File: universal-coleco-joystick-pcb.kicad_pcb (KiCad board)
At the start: 2 copper layers, 108 x 62.3 mm, 50 parts, among them J1 Sanwa Joystick, J2 DE9_Receptacle, J3 Conn_01x09_Socket, J4 Opt'l Numbers, SW1 Arm, SW10 2, SW11 #, SW12 9, SW13 6, SW14 3, SW2 Fire, SW3 *, SW4 7, SW5 1, SW6 4, SW7 0, SW8 8, SW9 5

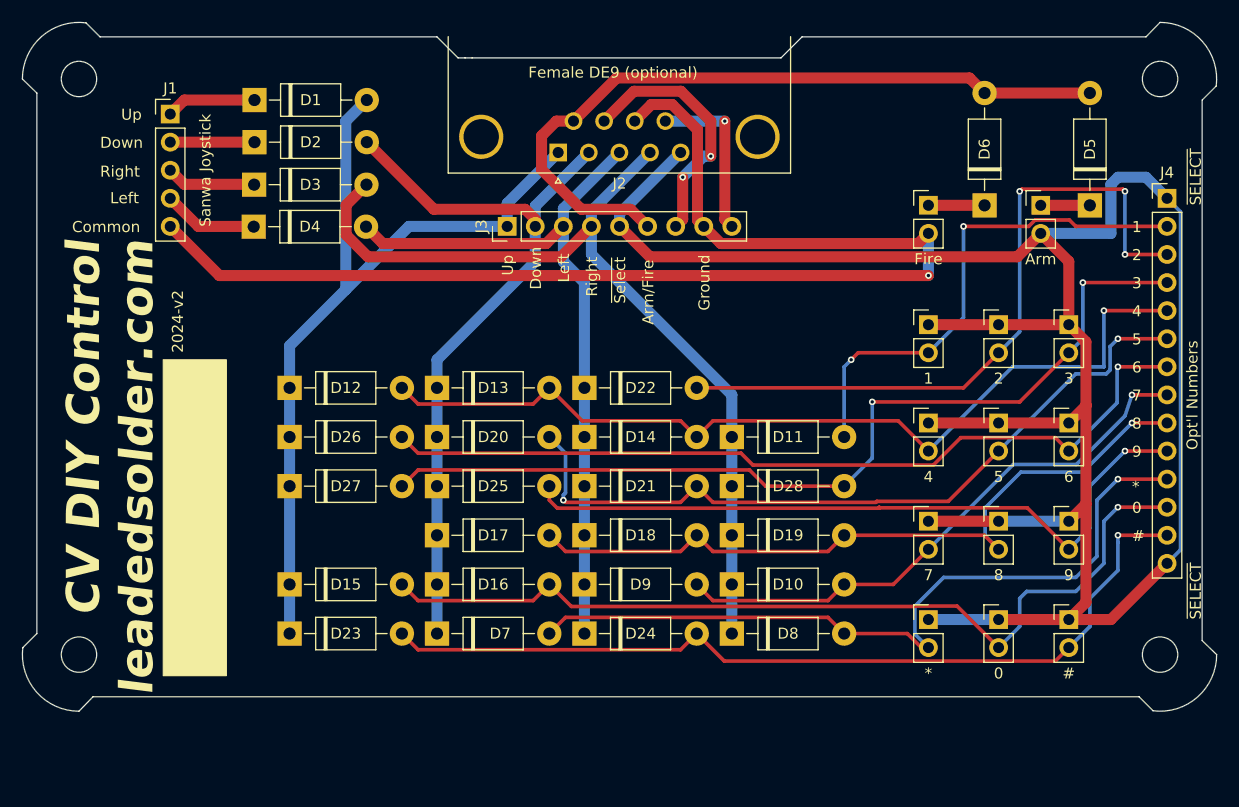
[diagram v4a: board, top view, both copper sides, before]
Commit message: Diodes flipped, board shrunk below 100x100
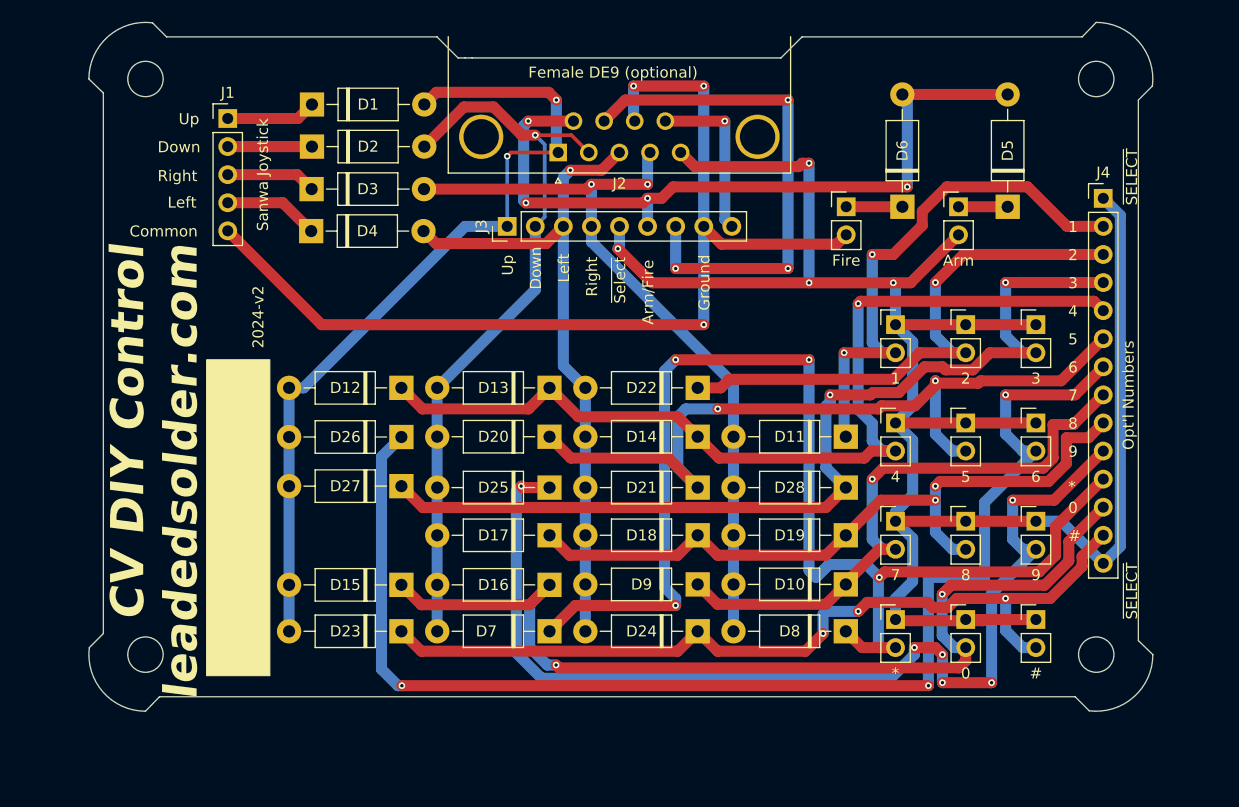
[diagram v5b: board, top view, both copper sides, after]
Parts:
- moved D8 10.3 mm to (156.4, 116.0), turned to 180 degrees
- moved D28 10.3 mm to (156.4, 103.0), turned to 180 degrees
- moved D11 10.3 mm to (156.4, 98.4), turned to 180 degrees
- moved D10 10.3 mm to (156.4, 111.8), turned to 180 degrees
- moved D19 10.3 mm to (156.4, 107.3), turned to 180 degrees
- moved D24 10.2 mm to (143.0, 116.0), turned to 180 degrees
- moved D21 10.2 mm to (143.0, 103.0), turned to 180 degrees
- moved D14 10.2 mm to (143.0, 98.4), turned to 180 degrees
- moved D18 10.2 mm to (143.0, 107.3), turned to 180 degrees
- moved D22 10.2 mm to (143.0, 94.0), turned to 180 degrees
- moved D9 10.2 mm to (143.0, 111.8), turned to 180 degrees
- moved D7 10.2 mm to (129.6, 116.0), turned to 180 degrees
- moved D25 10.2 mm to (129.6, 103.0), turned to 180 degrees
- moved D16 10.2 mm to (129.6, 111.8), turned to 180 degrees
- moved D20 10.2 mm to (129.6, 98.4), turned to 180 degrees
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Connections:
- D10 pad 1: /Right -> /KP_7
- D10 pad 2: /KP_7 -> /Right
- D11 pad 1: /Right -> /KP_1
- D11 pad 2: /KP_1 -> /Right
- D12 pad 1: /Up -> /KP_4
- D12 pad 2: /KP_4 -> /Up
- D13 pad 1: /Down -> /KP_4
- D13 pad 2: /KP_4 -> /Down
- D14 pad 1: /Left -> /KP_4
- D14 pad 2: /KP_4 -> /Left
- D15 pad 1: /Up -> /KP_0
- D15 pad 2: /KP_0 -> /Up
- D16 pad 1: /Down -> /KP_0
- D16 pad 2: /KP_0 -> /Down
- D17 pad 1: /Down -> /KP_8
- D17 pad 2: /KP_8 -> /Down
- D18 pad 1: /Left -> /KP_8
- D18 pad 2: /KP_8 -> /Left
- D19 pad 1: /Right -> /KP_8
- D19 pad 2: /KP_8 -> /Right
- D20 pad 1: /Down -> /KP_5
- D20 pad 2: /KP_5 -> /Down
- D21 pad 1: /Left -> /KP_5
- D21 pad 2: /KP_5 -> /Left
- D22 pad 1: /Left -> /KP_2
- D22 pad 2: /KP_2 -> /Left
- D23 pad 1: /Up -> /KP_OCTOTHORPE
- D23 pad 2: /KP_OCTOTHORPE -> /Up
- D24 pad 1: /Left -> /KP_OCTOTHORPE
- D24 pad 2: /KP_OCTOTHORPE -> /Left
- D25 pad 1: /Down -> /KP_9
- D25 pad 2: /KP_9 -> /Down
- D26 pad 1: /Up -> /KP_6
- D26 pad 2: /KP_6 -> /Up
- D27 pad 1: /Up -> /KP_3
- D27 pad 2: /KP_3 -> /Up
- D28 pad 1: /Right -> /KP_3
- D28 pad 2: /KP_3 -> /Right
- D7 pad 1: /Down -> /KP_STAR
- D7 pad 2: /KP_STAR -> /Down
- D8 pad 1: /Right -> /KP_STAR
- D8 pad 2: /KP_STAR -> /Right
- D9 pad 1: /Left -> /KP_7
- D9 pad 2: /KP_7 -> /Left
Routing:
- net /KP_STAR: track 70.8 -> 112.6 mm, vias 1 -> 4
- net /KP_6: track 76.8 -> 116.9 mm, vias 1 -> 3
- net /KP_9: track 65.0 -> 95.9 mm, vias 1 -> 6
- net /Quadrature_A: track 23.1 -> 46.6 mm, vias 2 -> 3
- net /Ground: track 111.8 -> 91.6 mm, vias 1 -> 3
- net /~{Select}: track 203.6 -> 189.7 mm, vias 0 -> 4
- net /KP_2: track 63.2 -> 50.0 mm, vias 3 -> 1
- net /Right: track 80.4 -> 69.1 mm, vias 0 -> 2
- net /KP_0: track 81.8 -> 88.2 mm, vias 1 -> 2
- net /KP_4: track 82.2 -> 87.2 mm
- net /KP_3: track 84.0 -> 88.5 mm
- net /Left: track 65.5 -> 61.7 mm, vias 0 -> 1
- net /KP_7: track 51.4 -> 54.6 mm
- net /KP_5: track 69.7 -> 72.4 mm
- net /KP_1: track 46.1 -> 48.4 mm
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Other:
- board size 108 x 62.3 mm -> 96.2 x 62.3 mm
